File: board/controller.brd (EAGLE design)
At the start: 100 x 100 mm, 33 parts, among them J1 X_SIG, J10 COOLANT, J12 VIN, J13 GND, J15 A_SIG, J16 +5V, J17 PROBE, J18 FEED_OVERRIDE, J19 MOTOR_CURRENT, J2 Y_SIG, J20 WHEEL, J21 IR_RECEIVER, J22 DISPLAY, J23 ERROR, J24 HOLDING, J25 SPINDLE, J26 SD_READER, J3 Z_SIG, J4 RESET, J5 Z_DISPLAY, J6 FEED_HOLD, J8 CYCLE_START

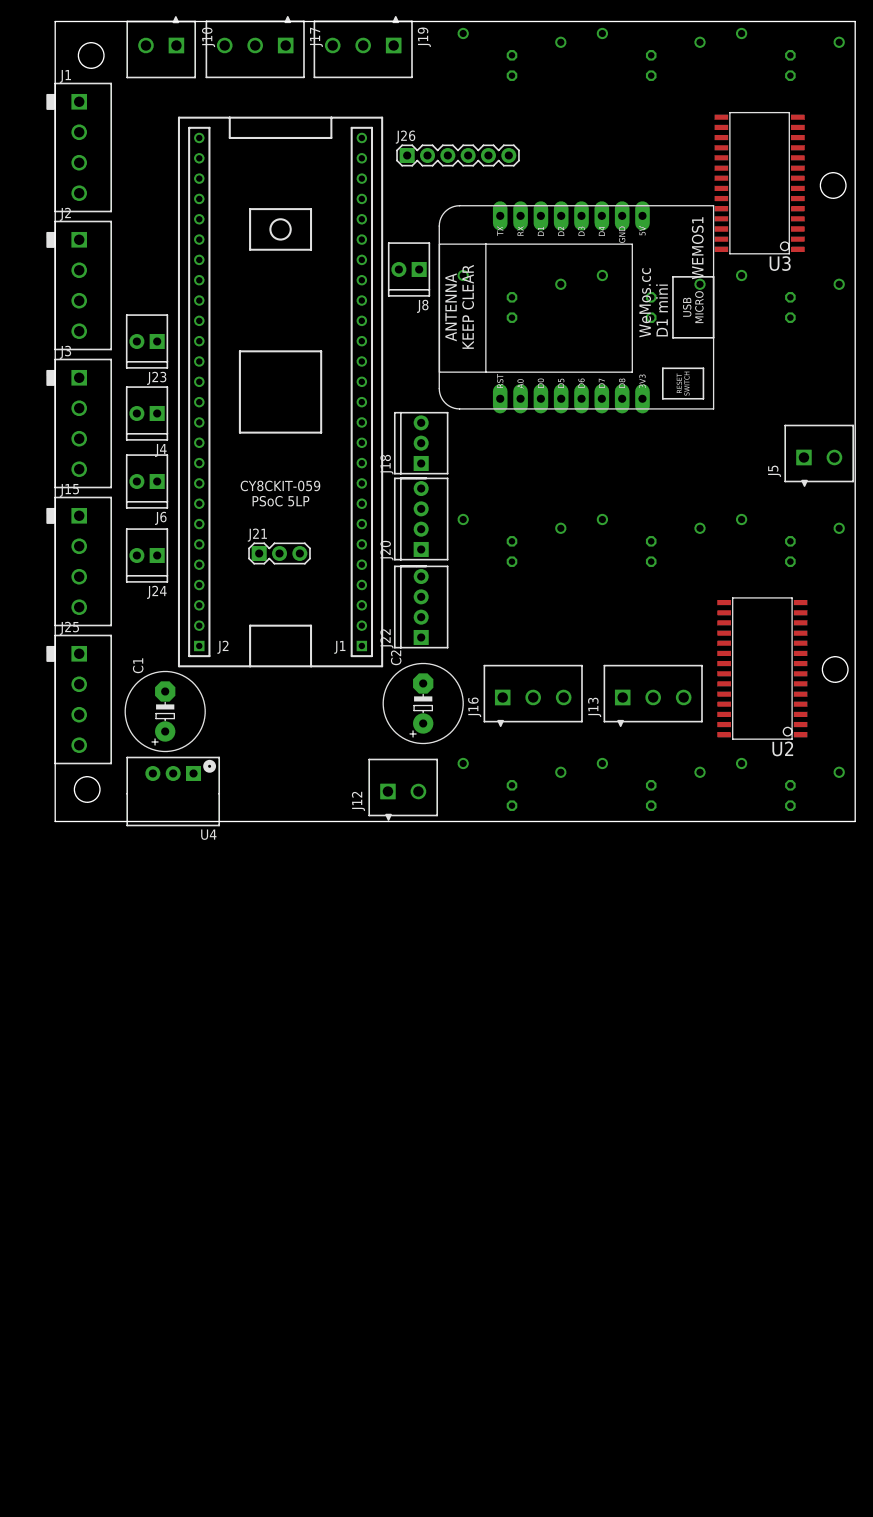
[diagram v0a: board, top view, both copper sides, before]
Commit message: started routing added datasheets
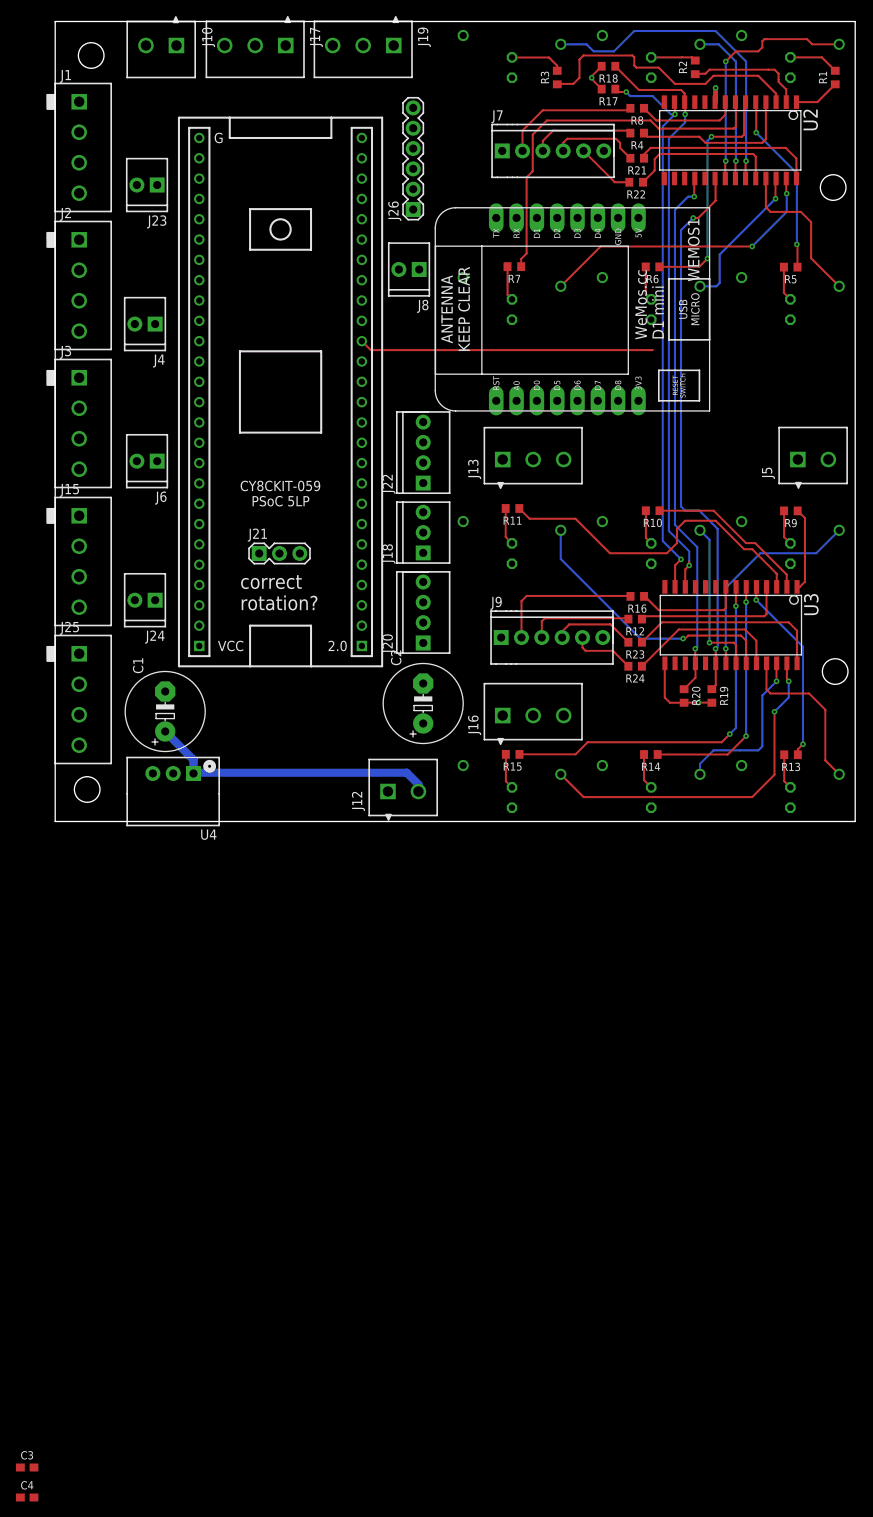
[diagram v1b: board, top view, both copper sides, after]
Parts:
- added C3, C4: (no value), holla:C0603
- added J7, J9: (no value), holla:CONN-.100-6
- added R1, R10, R11, R12, R13, R14, R15, R16, R2, R21, R22, R23, R24, R3, R4, R5, R6, R7, R8, R9: (no value), holla:R0603
- added R17, R18: 2.2k, holla:R0603
- added R19, R20: 10k, holla:R0603
- moved U2 66.8 mm to (85.0, 85.1), turned to 180 degrees
- moved U3 54.7 mm to (85.1, 24.5), turned to 180 degrees
- moved J13 33.3 mm to (59.8, 45.2)
- moved J23 19.6 mm to (12.8, 79.6)
- moved J22 19.3 mm to (46.0, 42.3)
- moved J20 11.7 mm to (46.0, 22.3)
- moved J18 11.2 mm to (46.0, 33.6)
- moved J4 11.2 mm to (12.5, 62.2)
- moved J26 6.79 mm to (44.8, 76.5), turned to 90 degrees
- moved J24 5.59 mm to (12.5, 27.7)
- moved J6 2.54 mm to (12.8, 45.0)
- moved J16 2.25 mm to (59.8, 13.2)
- moved J5 0.80 mm to (94.7, 45.2)
- moved WEMOS1 0.56 mm to (62.8, 62.7)
- moved S1 0.25 mm to (74.5, 94.2)
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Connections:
- removed net VDD: U2.9, U3.9
- removed net VSS: U2.10, U3.10
- new net !INT_IO: R19.1, U2.20, U3.20
- new net !RESET: R20.1, U2.18, U3.18
- new net N$1: R1.1, U2.1
- new net N$10: J9.5, R24.2
- new net N$11: J9.4, R23.2
- new net N$15: R3.1, U2.3
- new net N$16: R4.1, U2.4
- new net N$17: R5.1, U2.5
- new net N$18: R6.1, U2.6
- new net N$19: R7.1, U2.7
- new net N$2: R2.1, U2.2
- new net N$20: R8.1, U2.8
- new net N$21: R9.1, U3.1
- new net N$22: R10.1, U3.2
- new net N$23: R11.1, U3.3
- new net N$24: R12.1, U3.4
- new net N$25: R13.1, U3.5
- new net N$26: R14.1, U3.6
- new net N$27: R15.1, U3.7
- new net N$28: R16.1, U3.8
- new net N$3: R22.1, U2.24
- new net N$30: J7.2, R8.2
- new net N$4: J7.5, R22.2
- new net N$44: J9.3, R12.2
- new net N$48: J9.2, R16.2
- new net N$5: R21.1, U2.28
- new net N$6: J7.3, R4.2
- new net N$7: J7.4, R21.2
- new net N$8: R24.1, U3.24
- new net N$9: R23.1, U3.28
- new net S1A1: S1.A_1, U2.21
- new net S1AA: R1.2, S1.A_A
- new net S1B1: S1.B_1, U2.22
- new net S1BA: R2.2, S1.B_A
- new net S1C1: S1.C_1, U2.23
- new net S1CA: R3.2, S1.C_A
- new net S2A1: S2.A_1, U2.25
- new net S2AA: R5.2, S2.A_A
- new net S2B1: S2.B_1, U2.26
- new net S2BA: R6.2, S2.B_A
- new net S2C1: S2.C_1, U2.27
- new net S2CA: R7.2, S2.C_A
- new net S3A1: S3.A_1, U3.21
- new net S3AA: R9.2, S3.A_A
- new net S3B1: S3.B_1, U3.22
- new net S3BA: R10.2, S3.B_A
- new net S3C1: S3.C_1, U3.23
- new net S3CA: R11.2, S3.C_A
- new net S4A1: S4.A_1, U3.25
- new net S4AA: R13.2, S4.A_A
- new net S4B1: S4.B_1, U3.26
- new net S4BA: R14.2, S4.B_A
- new net S4C1: S4.C_1, U3.27
- new net S4CA: R15.2, S4.C_A
- net 5V0: now also C3.1, C4.1, J7.6, J9.6, R17.2, R18.2, R19.2, R20.2, U2.9, U3.15, U3.9
- net GND: now also C3.2, C4.2, J7.1, J9.1, S1.A_2, S1.A_C, S1.B_2, S1.B_C, S1.C_2, S1.C_C, S2.A_2, S2.A_C, S2.B_2, S2.B_C, S2.C_2, S2.C_C, S3.A_2, S3.A_C, S3.B_2, S3.B_C, S3.C_2, S3.C_C, S4.A_2, S4.A_C, S4.B_2, S4.B_C, S4.C_2, S4.C_C, U2.10, U2.15, U2.16, U2.17, U3.10, U3.16, U3.17
- net I2C_SCL: now also R18.1, U1.12.0, U2.12, U3.12
- net I2C_SDA: now also R17.1, U1.12.1, U2.13, U3.13
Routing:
- net I2C_SCL: track 0.00 -> 112.5 mm, vias 0 -> 2
- net I2C_SDA: track 0.00 -> 71.4 mm, vias 0 -> 3
- net !INT_IO: track 0.00 -> 69.3 mm, vias 0 -> 2
- net !RESET: track 0.00 -> 67.2 mm, vias 0 -> 2
- net N$19: track 0.00 -> 46.8 mm
- net N$27: track 0.00 -> 46.1 mm, vias 0 -> 2
- net S4C1: track 0.00 -> 43.8 mm, vias 0 -> 2
- net N$23: track 0.00 -> 41.6 mm
- net S1C1: track 0.00 -> 40.8 mm, vias 0 -> 1
- net VIN: track 0.00 -> 36.4 mm
- net S2C1: track 0.00 -> 36.3 mm, vias 0 -> 2
- net N$15: track 0.00 -> 34.7 mm
- net S3C1: track 0.00 -> 34.1 mm, vias 0 -> 1
- net S1A1: track 0.00 -> 30.7 mm, vias 0 -> 2
- net N$26: track 0.00 -> 30.7 mm, vias 0 -> 2
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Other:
- board text added: "correct rotation?"

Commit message: added datasheet continued routing
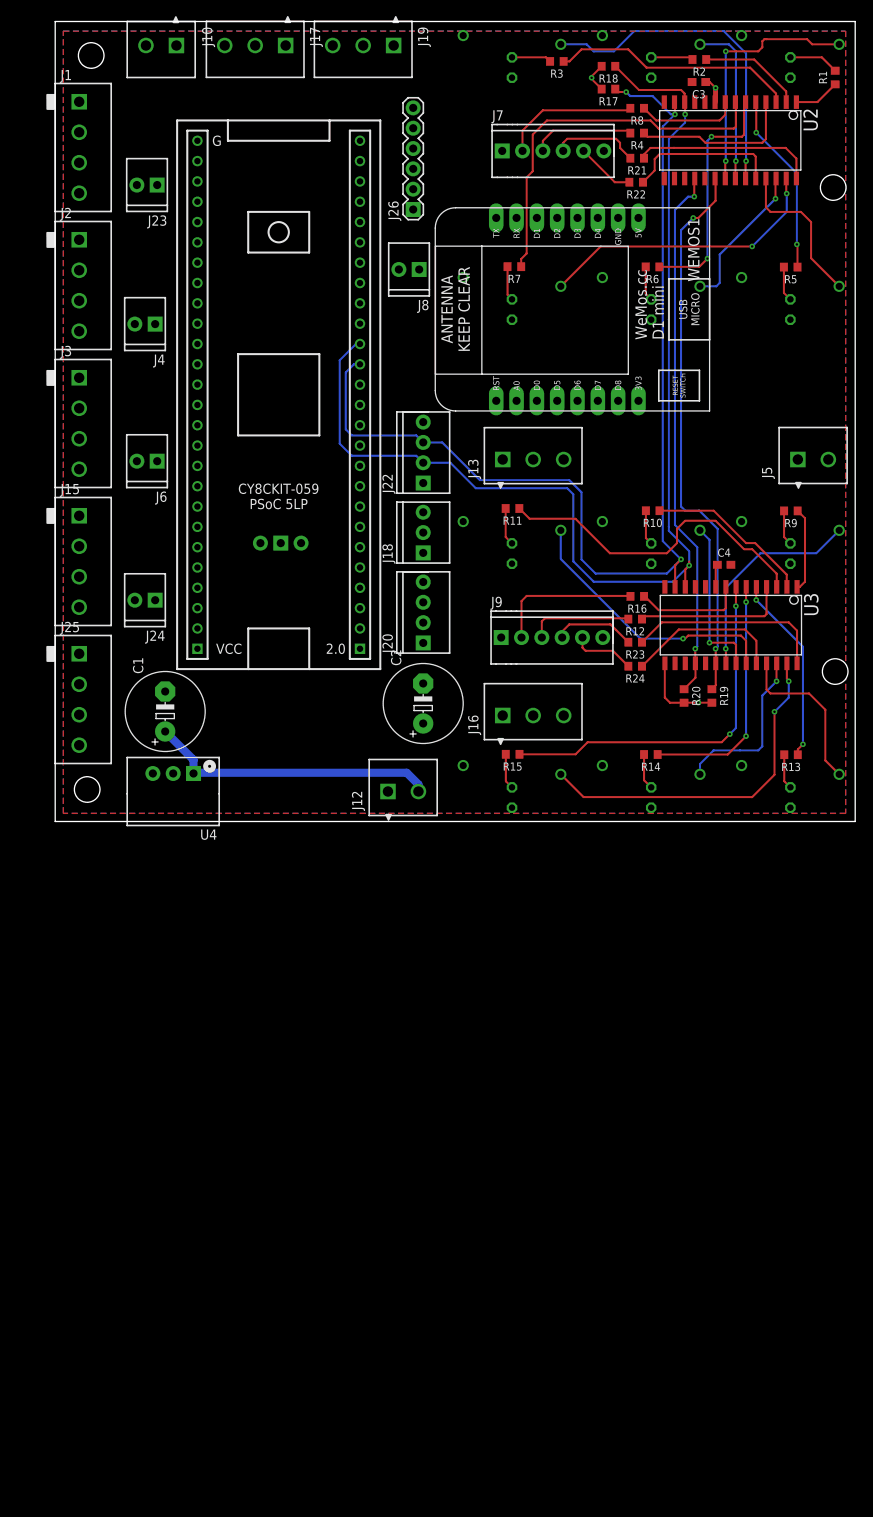
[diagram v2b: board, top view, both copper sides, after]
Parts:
- removed J21: IR_RECEIVER, holla:1X03
- added U5: SENSOR-IR-THRU, holla:IRDETECTOR-THRU
- moved C3 192.5 mm to (80.5, 92.4), turned to 180 degrees
- moved C4 145.5 mm to (83.6, 32.1)
- moved R3 2.01 mm to (62.7, 95.0), turned to 180 degrees
- moved R2 1.11 mm to (80.5, 95.2), turned to 180 degrees
- moved U1 0.42 mm to (27.9, 53.3)
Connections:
- new net N$34: U1.3.7
- new net N$35: U1.15.0
- new net N$36: U1.15.1
- new net N$37: U1.15.2
- new net N$38: U1.15.3
- new net N$39: U1.15.4
- new net N$40: U1.15.5
- new net N$41: U1.0.0
- new net N$42: U1.0.1
- new net N$43: U1.0.2
- new net N$45: U1.0.3
- net 5V0: now also U5.VCC; no longer J21.3
- net ERROR_INDICATOR_OUT: now also U1.3.2
- net GND: now also U5.GND; no longer J21.1
- net IR_RECEIVE_IN: now also U5.VOUT; no longer J21.2
- net X_DIRECTION_OUT: now also U1.3.3
- net X_LIMIT_IN: now also U1.3.0
- net X_STEP_OUT: now also U1.3.1
- net Y_DIRECTION_OUT: now also U1.3.6
- net Y_LIMIT_IN: now also U1.3.4
- net Y_STEP_OUT: now also U1.3.5
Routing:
- net I2C_SDA: track 71.4 -> 135.7 mm
- net I2C_SCL: track 112.5 -> 144.8 mm
- net 5V0: track 17.9 -> 22.3 mm
- net N$15: track 34.7 -> 30.5 mm
- net N$2: track 14.8 -> 13.0 mm
- net S1CA: track 6.71 -> 4.97 mm
- net S1A1: track 30.7 -> 31.4 mm
- net S1B1: track 20.1 -> 20.9 mm
- net S1C1: track 40.8 -> 41.4 mm
- added copper zone on layer 16, net 5V0
- added copper zone on layer 1, net GND
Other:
- board text removed: "correct rotation?"

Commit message: pin assignment and routing near completion
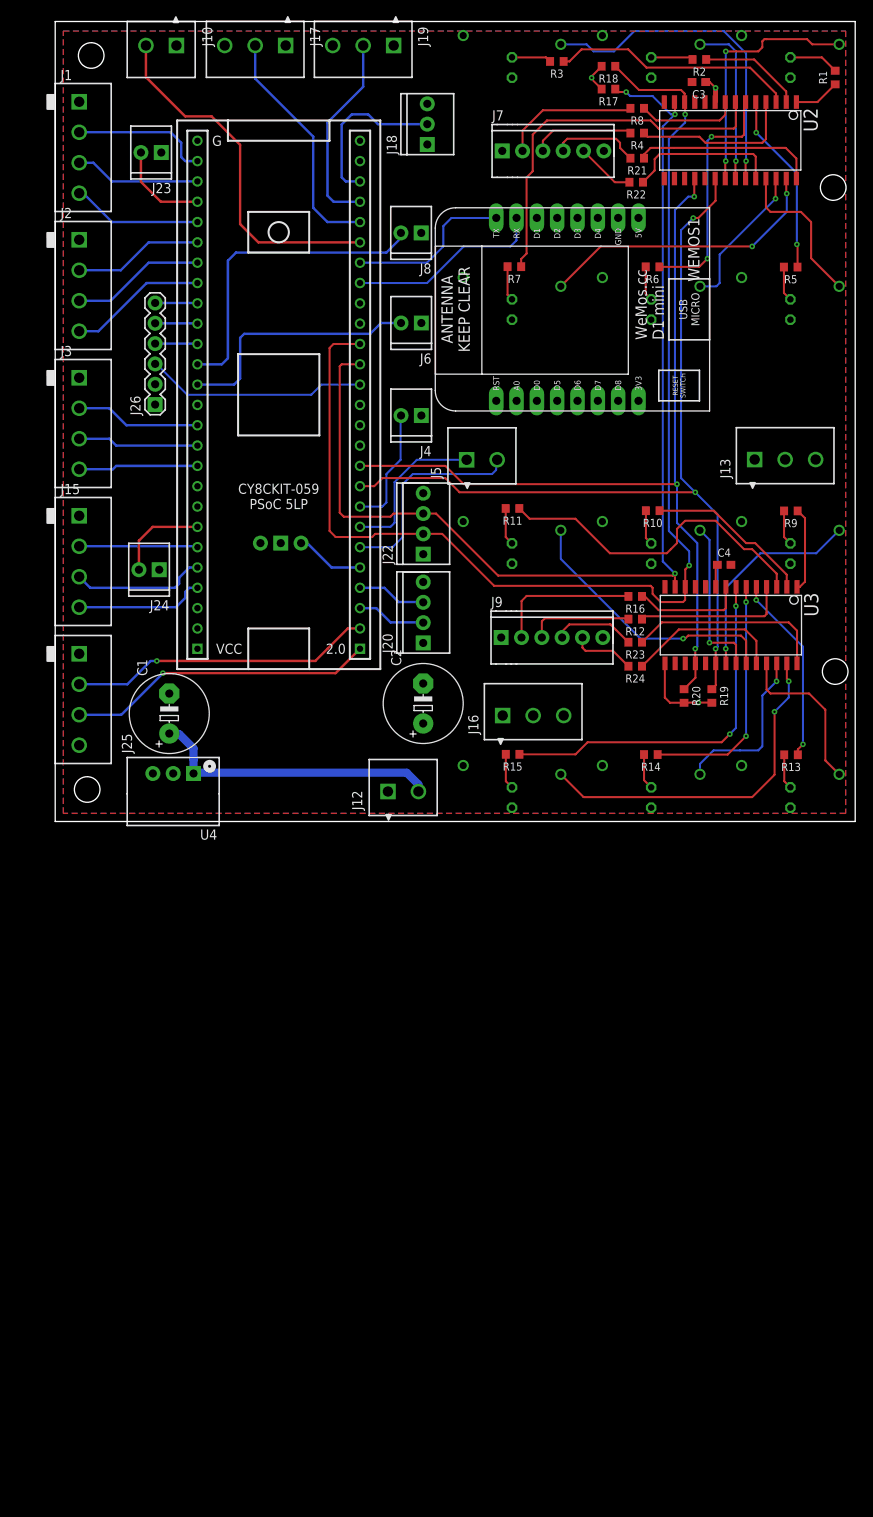
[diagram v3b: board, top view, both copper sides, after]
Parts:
- J1: value X_SIG -> X
- J15: value A_SIG -> A
- J2: value Y_SIG -> Y
- J3: value Z_SIG -> Z
- moved J18 51.1 mm to (46.5, 84.6)
- moved J5 41.4 mm to (53.3, 45.2)
- moved J26 40.4 mm to (12.5, 52.1)
- moved J6 37.3 mm to (45.8, 62.3)
- moved J4 35.2 mm to (45.8, 50.7)
- moved J13 31.5 mm to (91.2, 45.2)
- moved J22 8.89 mm to (46.0, 33.4)
- moved J8 4.58 mm to (45.8, 73.6)
- moved J23 4.10 mm to (13.3, 83.6)
- moved J24 3.84 mm to (13.0, 31.5)
- moved C1 0.57 mm to (14.3, 13.5)
- moved R16 0.25 mm to (72.5, 28.1)
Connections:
- removed net !INT_IO: R19.1, U2.20, U3.20
- removed net !RESET: R20.1, U2.18, U3.18
- removed net N$34: U1.3.7
- removed net N$35: U1.15.0
- removed net N$36: U1.15.1
- removed net N$37: U1.15.2
- removed net N$38: U1.15.3
- removed net N$40: U1.15.5
- removed net N$41: U1.0.0
- removed net N$42: U1.0.1
- new net !IO_INT: R19.1, U1.12.7, U2.20, U3.20
- new net !IO_RESET: R20.1, U1.12.6, U2.18, U3.18
- new net RADIO_RX: U1.1.2, WEMOS1.RX
- new net RADIO_TX: U1.1.3, WEMOS1.TX
- net 5V0: now also U1.VCC, WEMOS1.5V
- net A_DIRECTION_OUT: now also U1.0.7
- net A_LIMIT_IN: now also U1.0.5
- net A_STEP_OUT: now also U1.0.6
- net COOLANT_ENABLE_OUT: now also U1.1.4
- net CYCLE_START_IN: now also U1.15.2
- net FEED_HOLDING_OUT: now also U1.0.4
- net FEED_HOLD_IN: now also U1.15.3
- net FEED_OVERRIDE_IN: now also U1.1.7
- net GND: now also U1.GND@1, U1.GND@2, U1.GND@3, WEMOS1.GND
- net IR_RECEIVE_IN: now also U1.2.4
- net MOTOR_CURRENT_IN: now also U1.1.6
- net PROBE_IN: now also U1.1.5
- net RESET_IN: now also U1.2.7
- net SD_READER_CS: now also U1.15.1
- net SPINDLE_DIRECTION_OUT: now also U1.2.0
- net SPINDLE_ENABLE_OUT: now also U1.2.1
- net SPI_MISO: now also U1.3.7
- net SPI_MOSI: now also U1.12.2
- net SPI_SCK: now also U1.15.0
- net WHEEL_ENCODER_A_IN: now also U1.2.3
- net WHEEL_ENCODER_B_IN: now also U1.2.2
- net Z_DIRECTION_OUT: now also U1.0.1
- net Z_DISPLAY_RX_IN: now also U1.2.5
- net Z_DISPLAY_TX_OUT: now also U1.2.6
- net Z_LIMIT_IN: now also U1.15.5
- net Z_STEP_OUT: now also U1.0.0
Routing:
- net !IO_INT: track 0.00 -> 111.3 mm, vias 0 -> 3
- net !IO_RESET: track 0.00 -> 107.7 mm, vias 0 -> 3
- net !INT_IO: track 69.3 -> 0.00 mm, vias 2 -> 0
- net !RESET: track 67.2 -> 0.00 mm, vias 2 -> 0
- net COOLANT_ENABLE_OUT: track 0.00 -> 45.1 mm
- net CYCLE_START_IN: track 0.00 -> 39.8 mm
- net SPINDLE_DIRECTION_OUT: track 0.00 -> 38.5 mm, vias 0 -> 1
- net SPINDLE_ENABLE_OUT: track 0.00 -> 38.0 mm, vias 0 -> 1
- net FEED_HOLD_IN: track 0.00 -> 31.6 mm
- net PROBE_IN: track 0.00 -> 29.9 mm
- net SPI_MOSI: track 0.00 -> 27.7 mm
- net Z_DISPLAY_RX_IN: track 0.00 -> 26.2 mm
- net MOTOR_CURRENT_IN: track 0.00 -> 25.0 mm
- net RADIO_RX: track 0.00 -> 24.6 mm
- net RADIO_TX: track 0.00 -> 20.8 mm
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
